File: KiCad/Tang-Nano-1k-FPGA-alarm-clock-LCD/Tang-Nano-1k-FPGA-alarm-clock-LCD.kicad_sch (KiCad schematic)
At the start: 27 parts, among them Q1 PMOS, Q3 BC547, U1 LM2576T-5, U2 LM2903

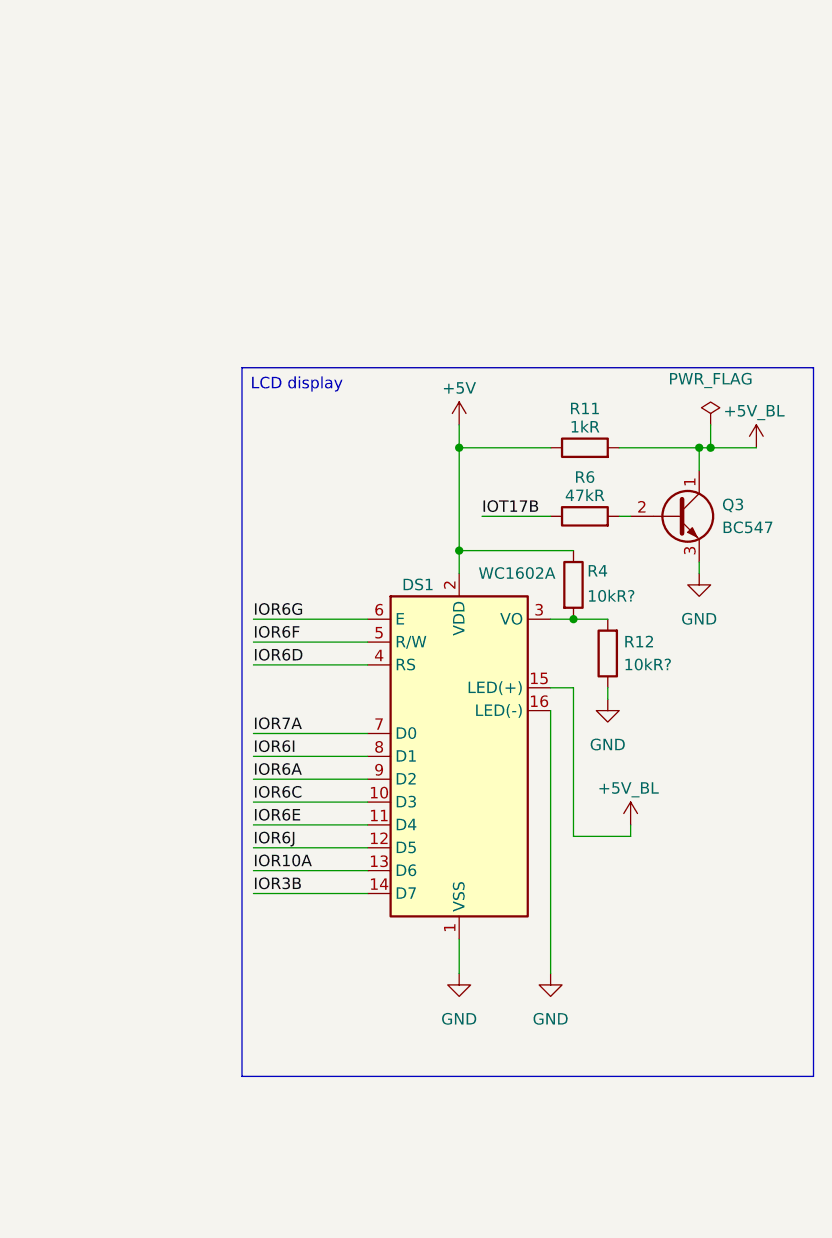
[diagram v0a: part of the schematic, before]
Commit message: alarm controller done
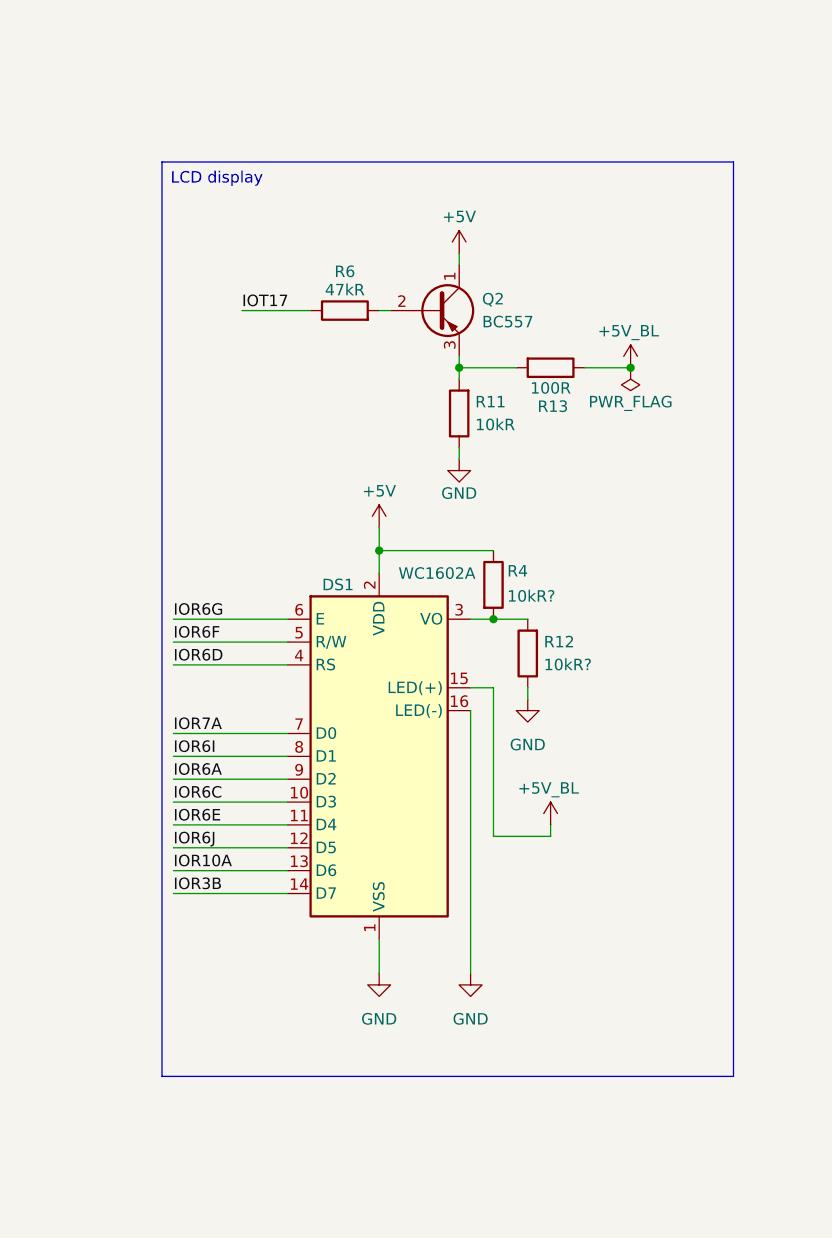
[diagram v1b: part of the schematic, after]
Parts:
- removed Q3: BC547, Package_TO_SOT_THT:TO-92_Inline, symbol Transistor_BJT:BC547
- added Q2: BC557, Package_TO_SOT_THT:TO-92_Inline, symbol Transistor_BJT:BC557
- added R13: 100R, Resistor_THT:R_Axial_DIN0207_L6.3mm_D2.5mm_P5.08mm_Vertical, symbol Device:R
- R11: value 1kR -> 10kR
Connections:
- net +5V: now also Q2.1 (C); no longer R11.1
- net +5V_BL: now also R13.1; no longer R11.2
- net GND: now also R11.1
- net IOT17B: no longer R6.1
- net at R6.2: now also Q2.2 (B)
- new net: Q2.3 (E), R11.2, R13.2
- new net IOT17: R6.1
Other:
- moved on the sheet: DS1, R12, R4, R6
